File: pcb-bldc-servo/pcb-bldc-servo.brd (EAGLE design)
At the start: 36.5 x 29 mm, 53 parts, among them J1 03-JST-B3B-XH-A, J2 03-JST-B3B-XH-A, J9 03-JST-B3B-XH-A, T1 MMBT2222, U1 AS5600, U2 STM32F030CCT6, X1 04-JST-B4B-XH-A, X2 PIN_6X1, X5 PIN_5X1HD

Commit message: updated gerber
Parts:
- moved V1 1.25 mm to (5.14, 24.0)
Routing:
- net GND: vias 71 -> 72
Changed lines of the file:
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@@
 <setting verticaltext="up"/>
 </settings>
-<grid distance="0.01" unitdist="mm" unit="mm" style="lines" multiple="1" display="no" altdistance="5" altunitdist="mil" altunit="mil"/>
+<grid distance="0.05" unitdist="mm" unit="mm" style="lines" multiple="1" display="no" altdistance="5" altunitdist="mil" altunit="mil"/>
 <layers>
 <layer number="1" name="Top" color="4" fill="1" visible="yes" active="yes"/>
@@
 <text x="32.8" y="13.96" size="1" layer="34" font="vector" ratio="10" rot="MR0">GND</text>
 <wire x1="27.03" y1="13.19" x2="21.98" y2="13.19" width="0.15" layer="34"/>
+<circle x="6.2" y="20.4" radius="0.6" width="0.1" layer="33"/>
+<wire x1="5.8" y1="20.4" x2="6.6" y2="20.4" width="0.1" layer="33"/>
+<circle x="11.65" y="21.75" radius="0.6" width="0.1" layer="33"/>
+<wire x1="11.25" y1="21.75" x2="12.05" y2="21.75" width="0.1" layer="33"/>
+<wire x1="11.65" y1="21.35" x2="11.65" y2="22.15" width="0.1" layer="33"/>
 </plain>
 <attributes>
@@
 <attribute name="NAME" x="17.778" y="22.61" size="1.016" layer="25" font="vector" ratio="12" rot="R90" align="bottom-center"/>
 </element>
-<element name="V1" library="ftobler" package="FIDUCIAL_2MM" value="FIDUCIAL2MM" x="5.23" y="22.76" smashed="yes"/>
+<element name="V1" library="ftobler" package="FIDUCIAL_2MM" value="FIDUCIAL2MM" x="5.14" y="24.01" smashed="yes"/>
 <element name="V2" library="ftobler" package="FIDUCIAL_2MM" value="FIDUCIAL2MM" x="32.58" y="25.81" smashed="yes"/>
 <element name="V3" library="ftobler" package="FIDUCIAL_2MM" value="FIDUCIAL2MM" x="32.68" y="2.99" smashed="yes"/>
@@
 <via x="9.505521875" y="9.614478125" extent="1-16" drill="0.3"/>
 <via x="34" y="14.45" extent="1-16" drill="0.8" diameter="1.5" shape="octagon"/>
+<via x="6.57" y="21.76" extent="1-16" drill="0.8" diameter="1.2" shape="octagon"/>
 </signal>
 <signal name="VCC" class="1">
@@
 <wire x1="31.35" y1="16.8" x2="31.35" y2="20.49" width="2" layer="15"/>
 <wire x1="31.35" y1="16.8" x2="22.65" y2="16.8" width="2" layer="15"/>
-<wire x1="18.7" y1="20.75" x2="8.85" y2="20.75" width="2" layer="15"/>
+<wire x1="18.7" y1="20.75" x2="10.25" y2="20.75" width="2" layer="15"/>
+<wire x1="10.25" y1="20.75" x2="8.85" y2="20.75" width="2" layer="15"/>
 <wire x1="22.65" y1="16.8" x2="18.7" y2="20.75" width="2" layer="15"/>
 <wire x1="12.9" y1="16" x2="12.4" y2="16" width="0.18" layer="1"/>
@@
 <wire x1="30.9" y1="9.8" x2="33.09" y2="11.99" width="0.2" layer="1"/>
 <via x="8.85" y="20.75" extent="1-16" drill="0.3"/>
-<via x="9.5" y="20.75" extent="1-16" drill="0.3"/>
 <via x="8.2" y="20.75" extent="1-16" drill="0.3"/>
 <polygon width="0.15" layer="1" thermals="no">
@@
 <wire x1="15.78" y1="19.39" x2="15.78" y2="21.03" width="0.15" layer="1"/>
 <wire x1="15.78" y1="21.03" x2="15.85" y2="21.1" width="0.15" layer="1"/>
+<via x="10.25" y="20.75" extent="1-16" drill="0.8" diameter="1.2"/>
 </signal>
 <signal name="NRST">

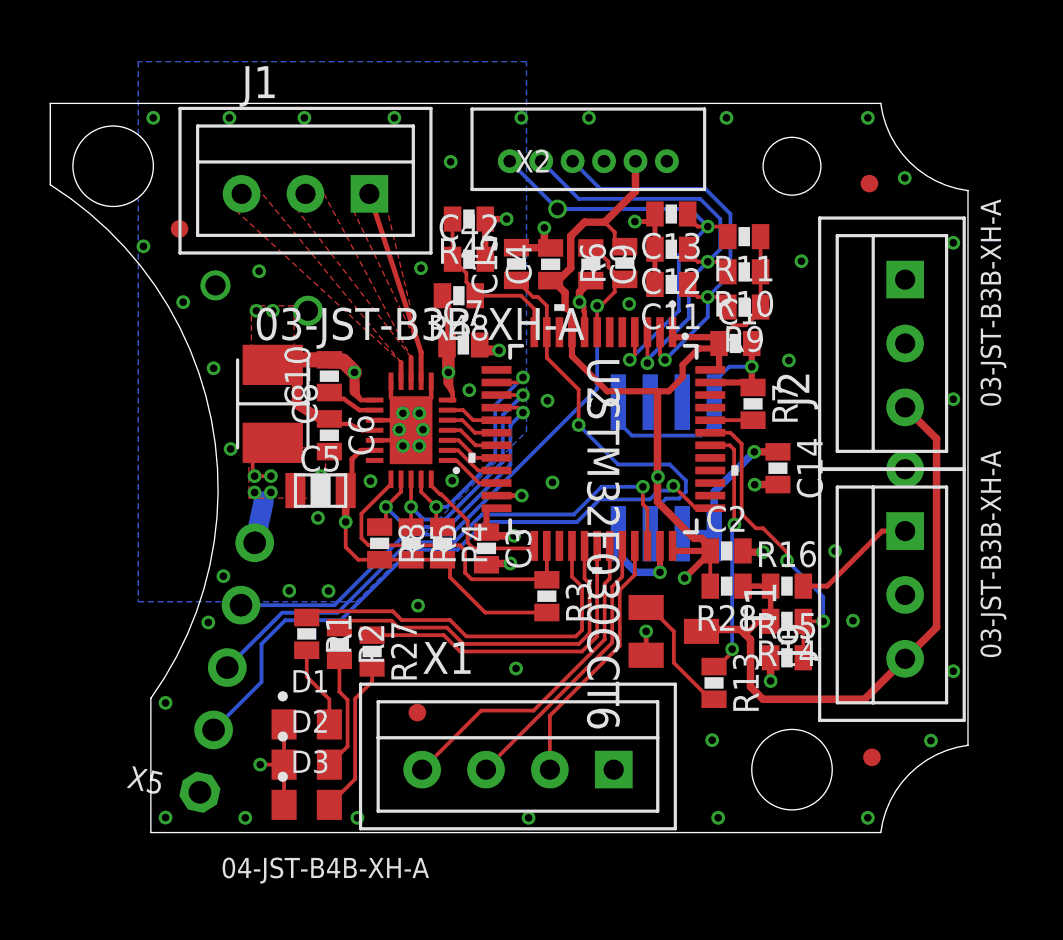
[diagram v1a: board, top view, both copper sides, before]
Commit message: updated schematic for correct sensor cable
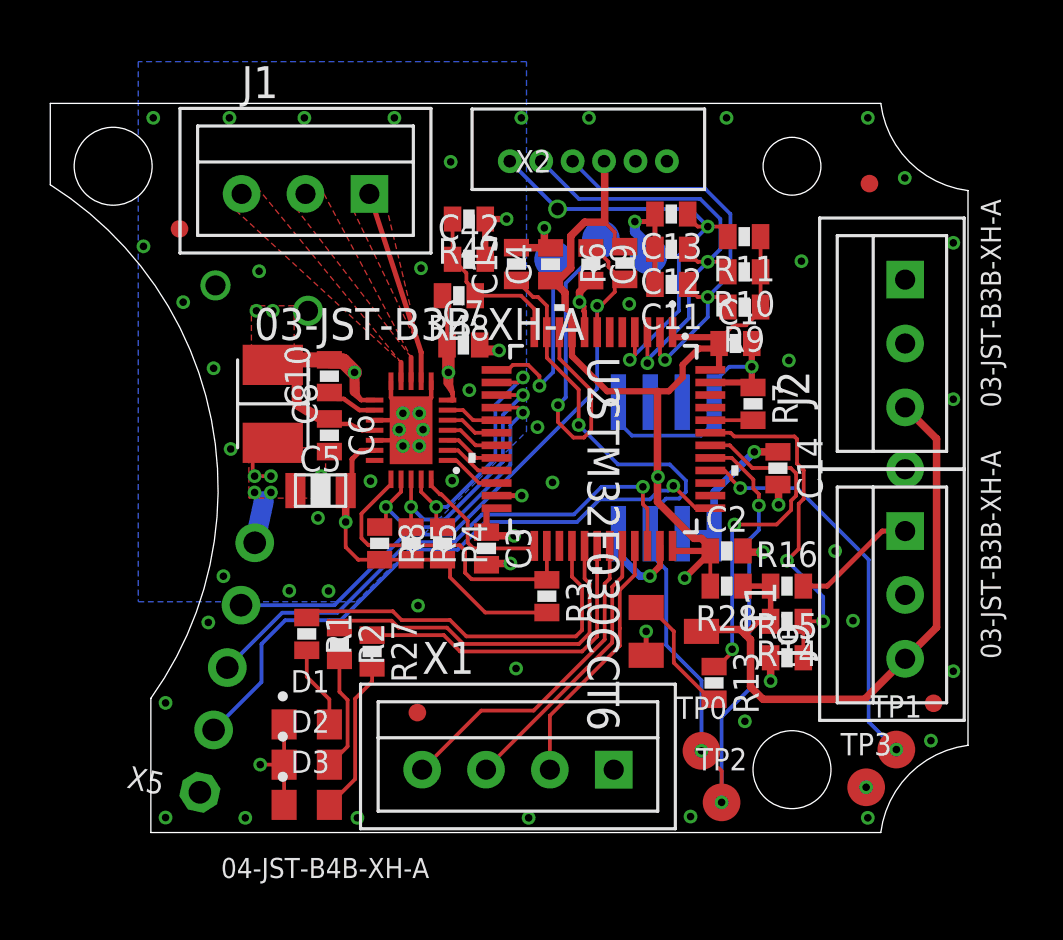
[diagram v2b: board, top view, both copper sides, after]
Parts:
- added TP0, TP1, TP2, TP3, TP4, TP5, TP6: TESTPIN, ftobler:PIN-SMD-1X1-TEST_1M5
- moved V3 3.26 mm to (35.1, 5.14)
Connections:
- new net N$31: TP1.1, U2.40
- new net N$33: TP2.1, U2.41
- new net N$34: TP4.1, U2.13
- new net N$35: TP5.1, U2.10
- net +3V3: now also X2.3; no longer X2.2
- net GND: now also TP3.1, TP6.1, X2.2; no longer X2.1
- net N$32: now also TP0.1
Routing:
- net N$33: track 0.00 -> 17.0 mm, vias 0 -> 2
- net N$31: track 0.00 -> 15.8 mm, vias 0 -> 2
- net N$35: track 0.00 -> 14.1 mm, vias 0 -> 1
- net N$32: track 15.1 -> 24.6 mm, vias 1 -> 2
- net N$34: track 0.00 -> 7.62 mm, vias 0 -> 1
- net N$12: track 10.1 -> 14.0 mm
- net N$13: track 12.4 -> 14.2 mm
- net GND: track 49.2 -> 50.7 mm, vias 72 -> 73
